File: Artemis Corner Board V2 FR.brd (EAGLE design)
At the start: 383.7 x 146 mm, 40 parts, among them U1 TPS562219, U10 TPS562219, U4 MCP2562FD

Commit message: Finally got shape right
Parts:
- added C72, C73: 10uF, adafruit:C0805
- added JP8: (no value), pinhead:1X02
- added LED6: GREEN, FormE:CHIPLED_0805
- added R15: 0.007, adafruit:R0805
- added R18: 1K, adafruit:R0805
- added U21: LM1085IS, FormE:TO-263
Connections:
- new net +12V: JP8.1, LED6.A
- new net 12V_CURRENT_SENSE+: C73.1, R15.1, U21.2, U21.GND, U21.GND1
- new net 12V_CURRENT_SENSE-: JP8.2, R15.2
- new net N$11: LED6.C, R18.2
- new net N$54: C72.1, U21.3
- net GND: now also C72.2, C73.2, R18.1, U21.1
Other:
- board size 383.7 x 146 mm -> 700.1 x 143.3 mm
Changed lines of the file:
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@@
 <wire x1="171.9834" y1="131.2926" x2="179.07" y2="19.431" width="0" layer="20"/>
 <wire x1="179.07" y1="19.431" x2="203.2" y2="0" width="0" layer="20" curve="180"/>
-<wire x1="307.4536375" y1="91.078621875" x2="381.702153125" y2="5.32990625" width="0" layer="20"/>
-<wire x1="381.702153125" y1="5.32990625" x2="374.371515625" y2="-8.47974375" width="0" layer="20" curve="-137.699407"/>
-<wire x1="374.371515625" y1="-8.47974375" x2="314.115459375" y2="-1.283440625" width="0" layer="20"/>
-<wire x1="314.115459375" y1="-1.283440625" x2="292.735" y2="22.802396875" width="0" layer="20" curve="-83.189496"/>
-<wire x1="292.735" y1="22.802396875" x2="292.735" y2="85.591825" width="0" layer="20"/>
-<wire x1="292.735" y1="85.591825" x2="307.4536375" y2="91.078621875" width="0" layer="20" curve="-139.111215"/>
+<wire x1="411.118621875" y1="13.4486375" x2="325.36990625" y2="87.697153125" width="0" layer="20"/>
+<wire x1="325.36990625" y1="87.697153125" x2="311.56025625" y2="80.366515625" width="0" layer="20" curve="137.699407"/>
+<wire x1="311.56025625" y1="80.366515625" x2="318.756559375" y2="20.110459375" width="0" layer="20"/>
+<wire x1="318.756559375" y1="20.110459375" x2="342.842396875" y2="-1.27" width="0" layer="20" curve="83.189496"/>
+<wire x1="342.842396875" y1="-1.27" x2="405.631825" y2="-1.27" width="0" layer="20"/>
+<wire x1="405.631825" y1="-1.27" x2="411.118621875" y2="13.4486375" width="0" layer="20" curve="139.111215"/>
+<wire x1="457.2" y1="0" x2="564.007" y2="0" width="0" layer="20"/>
+<wire x1="564.007" y1="0" x2="444.881" y2="114.980165625" width="0" layer="20"/>
+<wire x1="444.881" y1="114.980165625" x2="457.2" y2="0" width="0" layer="20"/>
+<wire x1="631.382671875" y1="0" x2="691.707003125" y2="0" width="0" layer="20"/>
+<wire x1="691.707003125" y1="0" x2="697.526234375" y2="14.414784375" width="0" layer="20" curve="136.032261"/>
+<wire x1="697.526234375" y1="14.414784375" x2="614.291265625" y2="94.70338125" width="0" layer="20"/>
+<wire x1="614.291265625" y1="94.70338125" x2="600.1383125" y2="87.77225" width="0" layer="20" curve="140.120308"/>
+<wire x1="600.1383125" y1="87.77225" x2="607.26539375" y2="21.657196875" width="0" layer="20"/>
+<wire x1="607.26539375" y1="21.657196875" x2="631.382671875" y2="0" width="0" layer="20" curve="83.847382"/>
 </plain>
 <attributes>
@@
 </element>
 <element name="H2" library="FormE" package="776228-4" value="776228-4" x="74.295" y="70.485"/>
+<element name="LED6" library="FormE" package="CHIPLED_0805" value="GREEN" x="-55.245" y="-24.765">
+<attribute name="PARTNO" value="598-8170-107F" x="-61.595" y="-3.81" size="1.778" layer="27" display="off"/>
+</element>
+<element name="R18" library="adafruit" package="R0805" value="1K" x="-43.815" y="-29.845">
+<attribute name="PARTNO" value="ERJ-6ENF1001V" x="-62.23" y="-8.89" size="1.778" layer="27" display="off"/>
+</element>
+<element name="R15" library="adafruit" package="R0805" value="0.007" x="-43.815" y="-22.225">
+<attribute name="PARTNO" value="PMR10EZPFU7L00" x="-62.23" y="-14.605" size="1.778" layer="27" display="off"/>
+</element>
+<element name="JP8" library="pinhead" package="1X02" value="" x="-48.895" y="-22.86"/>
+<element name="U21" library="FormE" package="TO-263" value="LM1085IS" x="-50.165" y="-12.7">
+<attribute name="PARTNO" value="LM1085IS-12/NOPB" x="-56.515" y="-29.845" size="1.778" layer="27" display="off"/>
+</element>
+<element name="C72" library="adafruit" package="C0805" value="10uF" x="-56.515" y="-29.845">
+<attribute name="PARTNO" value="GRM21BR61E106KA73L" x="-62.23" y="-39.37" size="1.778" layer="27" display="off"/>
+</element>
+<element name="C73" library="adafruit" package="C0805" value="10uF" x="-50.165" y="-29.845">
+<attribute name="PARTNO" value="GRM21BR61E106KA73L" x="-62.23" y="-45.085" size="1.778" layer="27" display="off"/>
+</element>
 </elements>
 <signals>
@@
 <wire x1="80.915" y1="35.83" x2="81.915" y2="36.83" width="0.4064" layer="1"/>
 <wire x1="81.915" y1="36.83" x2="81.915" y2="37.465" width="0.4064" layer="1"/>
+<contactref element="R18" pad="1"/>
+<contactref element="U21" pad="1"/>
+<contactref element="C72" pad="2"/>
+<contactref element="C73" pad="2"/>
 <wire x1="33.97" y1="66.04" x2="32.7025" y2="81.407" width="0" layer="19" extent="1-1"/>
 <wire x1="36.6522" y1="58.42" x2="33.97" y2="63.5" width="0" layer="19" extent="1-1"/>
 <wire x1="-46.0375" y1="18.542" x2="22.225" y2="19.685" width="0" layer="19" extent="1-1"/>
 <wire x1="-57.4675" y1="18.542" x2="-46.0375" y2="18.542" width="0" layer="19" extent="1-1"/>
+<wire x1="-43.815" y1="-15.24" x2="-46.0375" y2="18.542" width="0" layer="19" extent="1-1"/>
+<wire x1="-44.815" y1="-29.845" x2="-43.815" y2="-15.24" width="0" layer="19" extent="1-1"/>
+<wire x1="-49.315" y1="-29.845" x2="-44.815" y2="-29.845" width="0" layer="19" extent="1-1"/>
+<wire x1="-55.665" y1="-29.845" x2="-49.315" y2="-29.845" width="0" layer="19" extent="1-1"/>
 </signal>
 <signal name="+5V">
@@
 <via x="82.55" y="38.735" extent="1-16" drill="0.254" diameter="0.3048"/>
 </signal>
+<signal name="+12V">
+<contactref element="LED6" pad="A"/>
+<contactref element="JP8" pad="1"/>
+<wire x1="-50.165" y1="-22.86" x2="-55.245" y2="-25.815" width="0" layer="19" extent="1-1"/>
+</signal>
+<signal name="N$11">
+<contactref element="R18" pad="2"/>
+<contactref element="LED6" pad="C"/>
+<wire x1="-42.815" y1="-29.845" x2="-55.245" y2="-23.715" width="0" layer="19" extent="1-1"/>
+</signal>
+<signal name="12V_CURRENT_SENSE+">
+<contactref element="R15" pad="1"/>
+<contactref element="C73" pad="1"/>
+<contactref element="U21" pad="GND1"/>
+<contactref element="U21" pad="2"/>
+<contactref element="U21" pad="GND"/>
+<wire x1="-44.815" y1="-22.225" x2="-51.015" y2="-29.845" width="0" layer="19" extent="1-1"/>
+<wire x1="-43.815" y1="-12.7" x2="-44.815" y2="-22.225" width="0" layer="19" extent="1-1"/>
+<wire x1="-54.4957" y1="-12.7" x2="-43.815" y2="-12.7" width="0" layer="19" extent="1-1"/>
+<wire x1="-57.0357" y1="-12.7" x2="-54.4957" y2="-12.7" width="0" layer="19" extent="1-1"/>
+</signal>
+<signal name="12V_CURRENT_SENSE-">
+<contactref element="R15" pad="2"/>
+<contactref element="JP8" pad="2"/>
+<wire x1="-42.815" y1="-22.225" x2="-47.625" y2="-22.86" width="0" layer="19" extent="1-1"/>
+</signal>
+<signal name="N$54">
+<contactref element="U21" pad="3"/>
+<contactref element="C72" pad="1"/>
+<wire x1="-43.815" y1="-10.16" x2="-57.365" y2="-29.845" width="0" layer="19" extent="1-1"/>
+</signal>
 </signals>

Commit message: All regulators done, pin out for sealed connector almost done, need outs for image sensor
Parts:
- removed JP8: (no value), pinhead:1X02
- added C10, C11: 10uF, adafruit:C0805
- added C18: 8200pF, adafruit:C0805
- added C21, C9: 0.1uF, adafruit:C0805
- added C24, C25, C26: 22uF, adafruit:C0805
- added L3: 4.7uH, FormE:SRP6540
- added LED7: GREEN, FormE:CHIPLED_0805
- added R10, R6, R8: 10K, adafruit:R0805
- added R5: 26.1K, adafruit:R0805
- added R9: 1K, adafruit:R0805
- added U3: TPS562219, FormE:TPS562219
- R24: value 54.9k -> 5.76K
- moved C22 128.2 mm to (50.2, -61.0)
- moved C23 128.2 mm to (50.2, -63.5)
- moved LED1 128.2 mm to (50.2, -46.4)
- moved R7 128.2 mm to (44.5, -67.9)
- moved U4 128.2 mm to (51.4, -67.9)
- moved C13 115.0 mm to (20.3, -62.9)
- moved C12 115.0 mm to (17.8, -62.9)
- moved C14 115.0 mm to (22.9, -62.9)
- moved C15 115.0 mm to (8.89, -59.1)
- moved C16 115.0 mm to (9.53, -67.3)
- moved C17 115.0 mm to (17.1, -76.2)
- moved C19 115.0 mm to (17.1, -73.7)
- moved C20 115.0 mm to (17.1, -71.1)
- moved L2 115.0 mm to (9.53, -74.3)
- moved LED3 115.0 mm to (15.2, -78.7)
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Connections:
- removed net 12V_CURRENT_SENSE-: JP8.2, R15.2
- removed net N$54: C72.1, U21.3
- removed net N$6: U2.9
- removed net N$7: U2.58
- removed net N$8: U2.62
- new net +1V2: C17.1, C19.1, C20.1, C23.1, L2.P$2, LED3.A, R24.2, U2.11, U2.2, U2.26, U2.42, U2.54, U4.5
- new net +2V8: C24.1, C25.1, C26.1, L3.P$2, LED7.A, R5.2
- new net DAMPER_POS_OUT: H2.P$23, U2.17
- new net SS_5V2: C18.1, U3.5
- new net STRAIN_GADGE_VOLTMETER_IN_0: H2.P$19, U2.6, U2.8
- new net STRAIN_GADGE_VOLTMETER_IN_1: H2.P$18, U2.7
- new net STRAIN_GAUGE_VOLTMETER_OUT: H2.P$17, U2.28
- new net SW_5V2: C21.2, L3.P$1, U3.2
- new net VBST_5V2: C21.1, U3.8
- new net VFB_5V2: R5.1, R6.2, U3.6
- new net WHEEL_SPEED_OUT: R10.1, U2.21
- net +12V: now also H2.P$1, H2.P$16, H2.P$9, R10.2, R15.2; no longer JP8.1
- net +3V3: now also H2.P$7, H2.P$8; no longer C23.1, U2.11, U2.2, U2.26, U2.42, U2.54, U4.5
- net +5V: no longer C17.1, C19.1, C20.1, L2.P$2, LED3.A, R24.2
- net GND: now also C10.2, C11.2, C18.2, C24.2, C25.2, C26.2, C9.2, H2.P$2, H2.P$3, H2.P$4, H2.P$5, H2.P$6, R6.1, R9.1, U3.1
- net N$3: now also LED7.C, R9.2; no longer U2.6
- net N$4: now also R8.2, U3.7; no longer U2.7
- net N$5: now also H2.P$10; no longer U2.8
- net PROGRAMMING_CAN_N: now also H2.P$22
- net PROGRAMMING_CAN_P: now also H2.P$21
- net PROGRAMMING_CAN_RX: now also U2.58; no longer U2.28
- net VCC: now also C10.1, C11.1, C72.1, C9.1, H2.P$20, R8.1, U21.3, U3.3
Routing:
- net +1V2: track 0.00 -> 11.0 mm, vias 0 -> 4
- net +3V3: track 12.6 -> 1.54 mm, vias 10 -> 6
- net N$4: track 0.00 -> 7.10 mm, vias 0 -> 2
- net GND: track 29.5 -> 36.6 mm, vias 38 -> 53
- net VFB_5V2: track 0.00 -> 6.85 mm
- net PROGRAMMING_CAN_RX: track 10.0 -> 4.89 mm
- net VBST_5V2: track 0.00 -> 3.33 mm
- net VCC: track 5.41 -> 8.44 mm, vias 12 -> 27
- net 12V_CURRENT_SENSE+: track 0.00 -> 2.69 mm
- net SS_5V2: track 0.00 -> 2.66 mm
- net +5V: track 6.11 -> 3.67 mm, vias 9 -> 8
- net N$3: track 0.00 -> 2.39 mm
- net SW_5V2: track 0.00 -> 1.75 mm, vias 0 -> 6
- net +2V8: track 0.00 -> 1.54 mm, vias 0 -> 6
- added copper zone on layer 1, net +12V
- added copper zone on layer 15, net +12V
- added copper zone on layer 1, net +2V8
- added copper zone on layer 1, net 12V_CURRENT_SENSE+
- added copper zone on layer 1, net SW_5V2
- added copper zone on layer 16, net SW_5V2
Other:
- board size 700.1 x 143.3 mm -> 132.4 x 63.1 mm

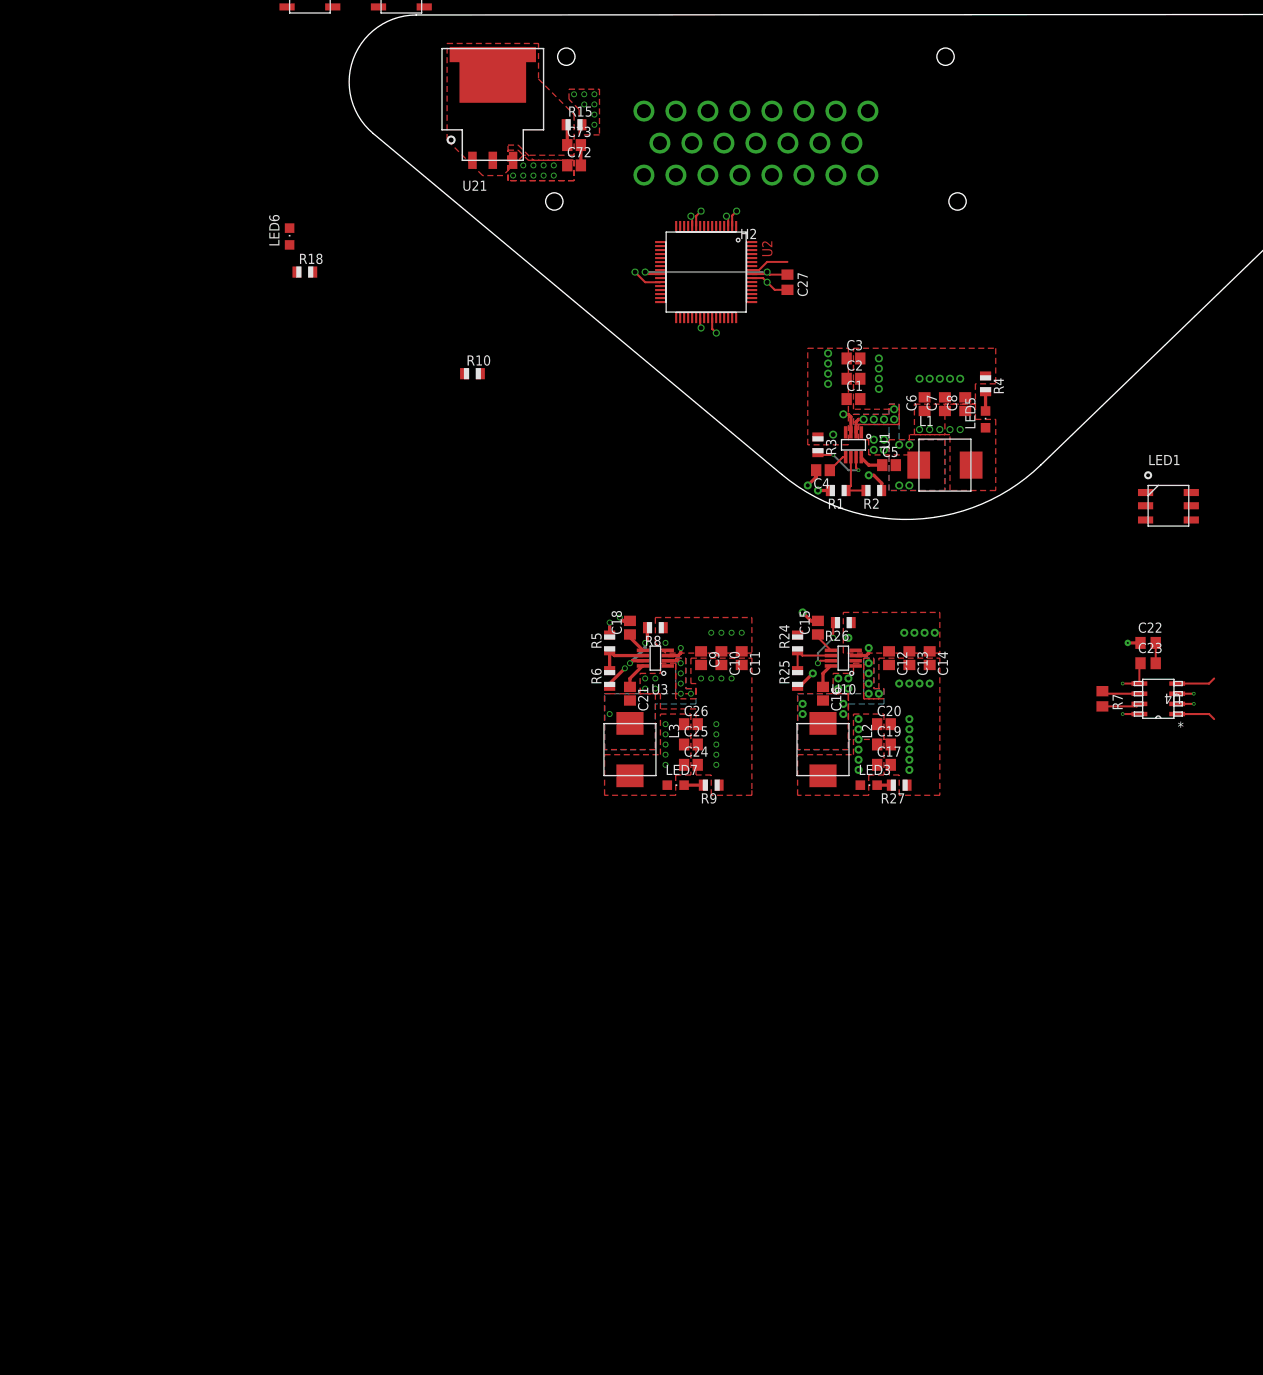
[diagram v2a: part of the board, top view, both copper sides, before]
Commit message: About to delete 1V2 and 2V8 Regulators because switching Image sensor
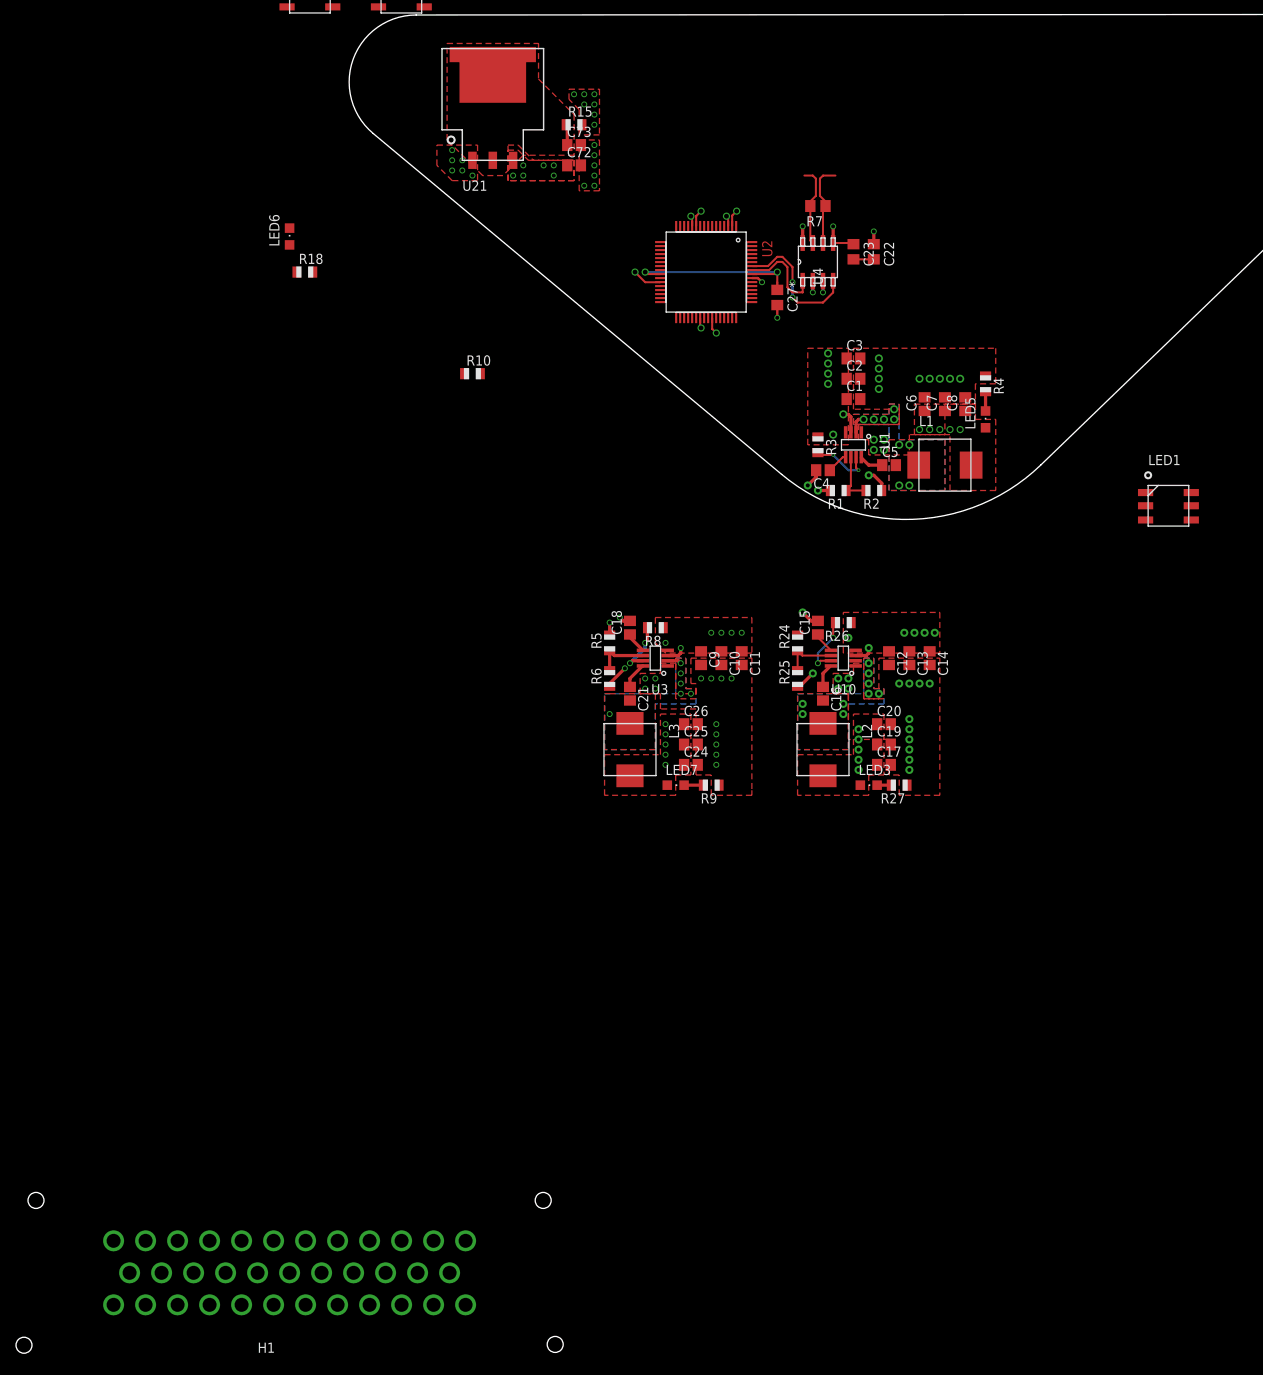
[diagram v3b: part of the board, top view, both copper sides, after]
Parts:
- removed H2: 776228-4, FormE:776228-4
- added H1: 1-776231-1, FormE:1-776231-1
- moved R7 71.1 mm to (8.89, -6.35), turned to 180 degrees
- moved U4 69.2 mm to (8.89, -13.3), turned to 90 degrees
- moved C23 63.3 mm to (13.3, -12.1), turned to 270 degrees
- moved C22 59.7 mm to (15.9, -12.1), turned to 270 degrees
- moved C27 2.29 mm to (3.81, -17.8)
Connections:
- removed net N$5: H2.P$10
- net +12V: now also H1.1, H1.21, H1.28; no longer H2.P$1, H2.P$16, H2.P$9
- net +3V3: now also H1.7, H1.8; no longer H2.P$7, H2.P$8
- net DAMPER_POS_OUT: now also H1.35; no longer H2.P$23
- net GND: now also H1.2, H1.3, H1.4, H1.5, H1.6; no longer H2.P$2, H2.P$3, H2.P$4, H2.P$5, H2.P$6
- net PROGRAMMING_CAN_N: now also H1.34; no longer H2.P$22
- net PROGRAMMING_CAN_P: now also H1.33; no longer H2.P$21
- net STRAIN_GADGE_VOLTMETER_IN_0: now also H1.31; no longer H2.P$19
- net STRAIN_GADGE_VOLTMETER_IN_1: now also H1.30; no longer H2.P$18
- net STRAIN_GAUGE_VOLTMETER_OUT: now also H1.29; no longer H2.P$17
- net VCC: now also H1.32; no longer H2.P$20
- net WHEEL_SPEED_OUT: now also H1.22
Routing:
- net PROGRAMMING_CAN_RX: track 4.89 -> 17.2 mm, vias 0 -> 2
- net PROGRAMMING_CAN_N: track 4.75 -> 10.6 mm
- net PROGRAMMING_CAN_P: track 4.75 -> 10.1 mm
- net GND: track 36.6 -> 31.4 mm, vias 53 -> 66
- net P$40: track 21.9 -> 24.0 mm
- net PROGRAMMING_CAN_TX: track 9.72 -> 11.3 mm
- net +5V: track 3.67 -> 3.04 mm, vias 8 -> 7
- net VCC: vias 27 -> 24
